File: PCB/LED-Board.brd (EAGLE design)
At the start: 71 x 34 mm, 33 parts, among them U1 ATSAMD11C14A-SSUT, U3 LDL1117S12R

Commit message: added button to pcbs and did some fixing
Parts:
- added R3: 2k, SparkFun-Resistors:1206
- added S1: MOMENTARY-SWITCH-SPST-SMD-6.0X3.5MM, SparkFun-Switches:TACTILE_SWITCH_SMD_6.0X3.5MM
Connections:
- removed net N$10: J3.4, U1.1
- new net N$13: J3.4, R3.2, S1.1, U1.1
- net 3.3V: now also S1.2
- net GND: now also R3.1
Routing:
- net N$13: track 0.00 -> 54.0 mm, vias 0 -> 3
- net 3.3V: track 55.3 -> 82.2 mm, vias 0 -> 4
- net N$10: track 20.9 -> 0.00 mm, vias 1 -> 0
- net VCC: track 58.8 -> 61.7 mm
- net N$2: track 24.5 -> 26.5 mm

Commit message: removed buttons.. not needed
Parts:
- removed R3: 2k, SparkFun-Resistors:1206
- removed S1: MOMENTARY-SWITCH-SPST-SMD-6.0X3.5MM, SparkFun-Switches:TACTILE_SWITCH_SMD_6.0X3.5MM
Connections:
- net 3.3V: no longer S1.2
- net GND: no longer R3.1
- net N$13: no longer R3.2, S1.1
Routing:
- net N$13: track 54.0 -> 20.9 mm, vias 3 -> 1
- net 3.3V: track 82.2 -> 62.5 mm, vias 4 -> 2

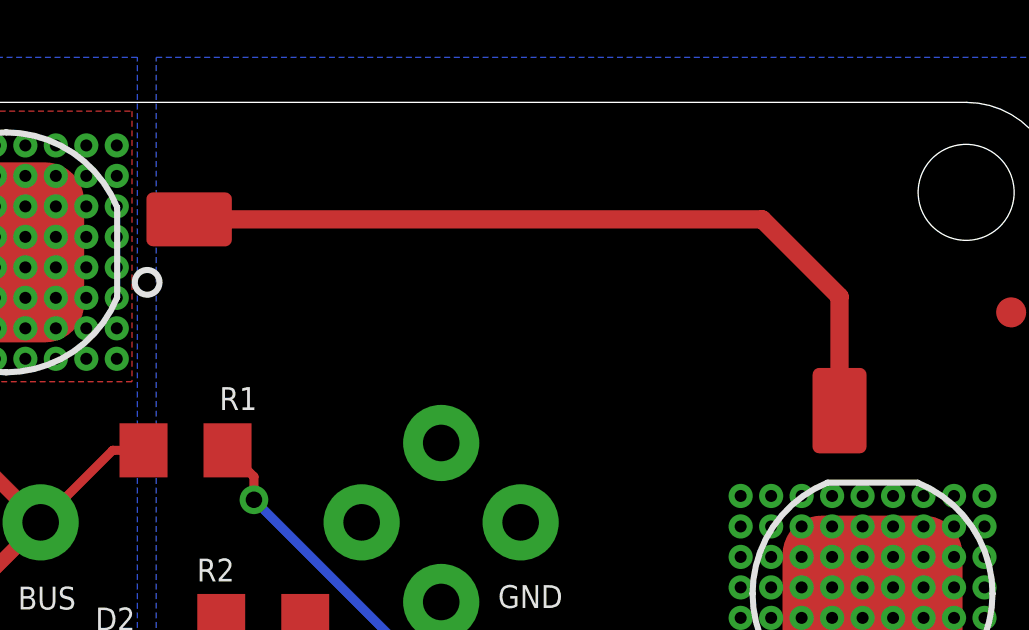
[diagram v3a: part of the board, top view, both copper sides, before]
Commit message: added b/tstop and b/restricted to write address on pcb
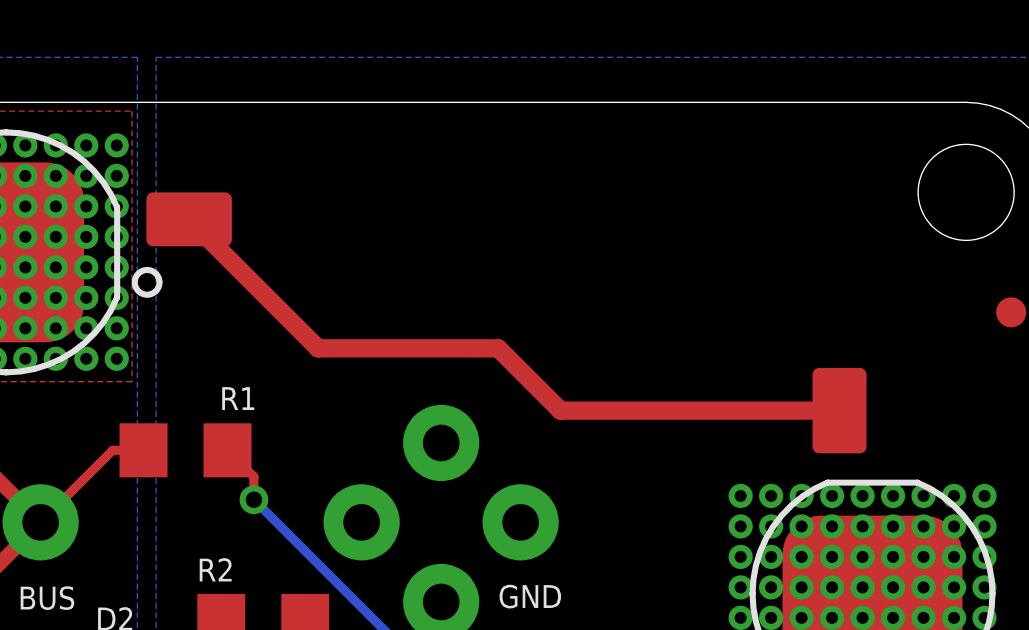
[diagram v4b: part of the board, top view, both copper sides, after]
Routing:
- net N$2: track 26.5 -> 24.3 mm
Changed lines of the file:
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@@
 <vertex x="9.31" y="15.241"/>
+</polygon>
+<polygon width="0.127" layer="30">
+<vertex x="47.141" y="33.207"/>
+<vertex x="64.496" y="33.207"/>
+<vertex x="64.496" y="26.99"/>
+<vertex x="47.141" y="26.99"/>
+</polygon>
+<polygon width="0.127" layer="41">
+<vertex x="64.459" y="33.207"/>
+<vertex x="47.104" y="33.207"/>
+<vertex x="47.104" y="26.99"/>
+<vertex x="64.459" y="26.99"/>
+</polygon>
+<polygon width="0.127" layer="29">
+<vertex x="64.459" y="33.207"/>
+<vertex x="47.104" y="33.207"/>
+<vertex x="47.104" y="26.99"/>
+<vertex x="64.459" y="26.99"/>
+</polygon>
+<polygon width="0.127" layer="42">
+<vertex x="64.459" y="26.993"/>
+<vertex x="47.104" y="26.993"/>
+<vertex x="47.104" y="33.21"/>
+<vertex x="64.459" y="33.21"/>
 </polygon>
 </plain>
@@
 <contactref element="LED-1" pad="C"/>
 <contactref element="LED-2" pad="A"/>
-<wire x1="42.1" y1="30.1" x2="61.203" y2="30.1" width="0.6096" layer="1"/>
-<wire x1="61.203" y1="30.1" x2="63.779" y2="27.524" width="0.6096" layer="1"/>
-<wire x1="63.779" y1="27.524" x2="63.779" y2="23.725" width="0.6096" layer="1"/>
-<wire x1="63.779" y1="23.725" x2="63.78" y2="23.724" width="0.6096" layer="1"/>
+<wire x1="52.404" y1="25.8" x2="46.4" y2="25.8" width="0.6096" layer="1"/>
+<wire x1="42.1" y1="30.1" x2="46.4" y2="25.8" width="0.6096" layer="1"/>
+<wire x1="54.48" y1="23.724" x2="63.78" y2="23.724" width="0.6096" layer="1"/>
+<wire x1="54.48" y1="23.724" x2="52.404" y2="25.8" width="0.6096" layer="1"/>
 </signal>
 <signal name="N$3">

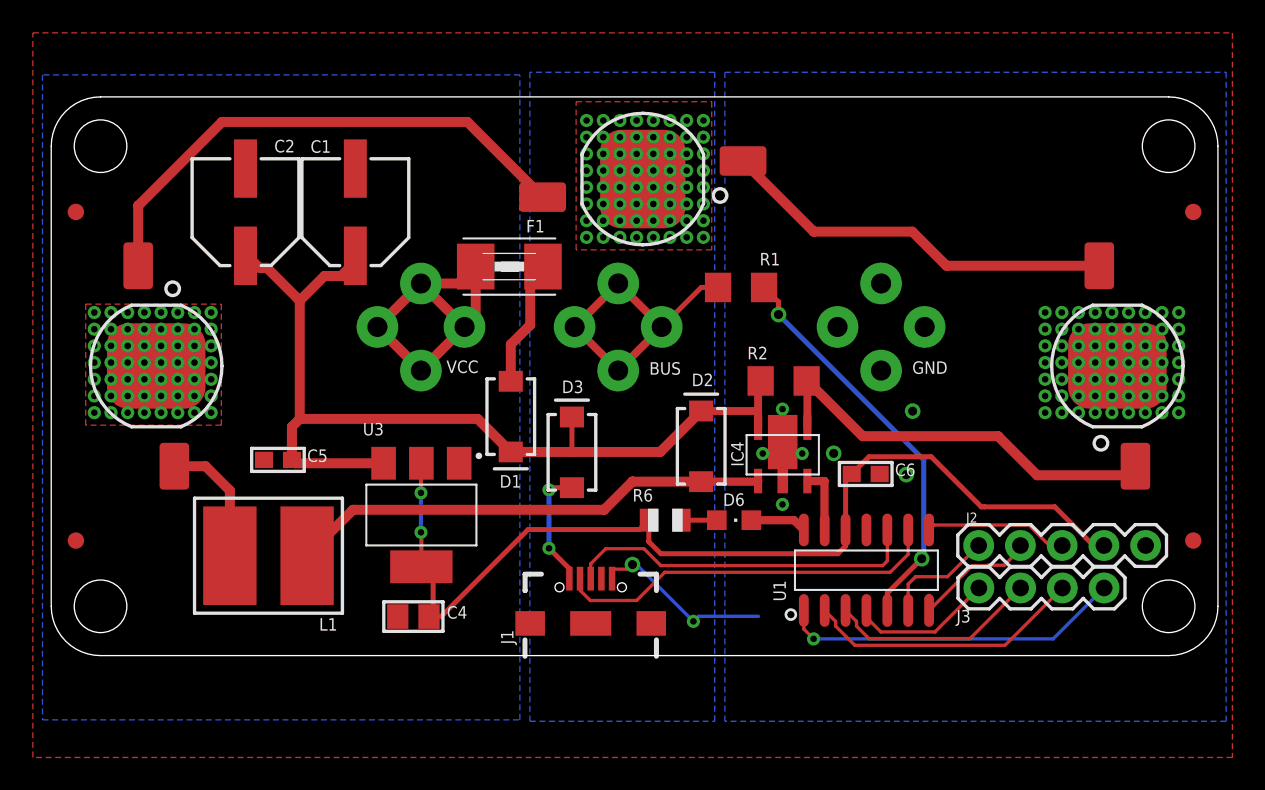
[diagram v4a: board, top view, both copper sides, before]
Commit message: increased led board bottom polygons for more equal heatsinks
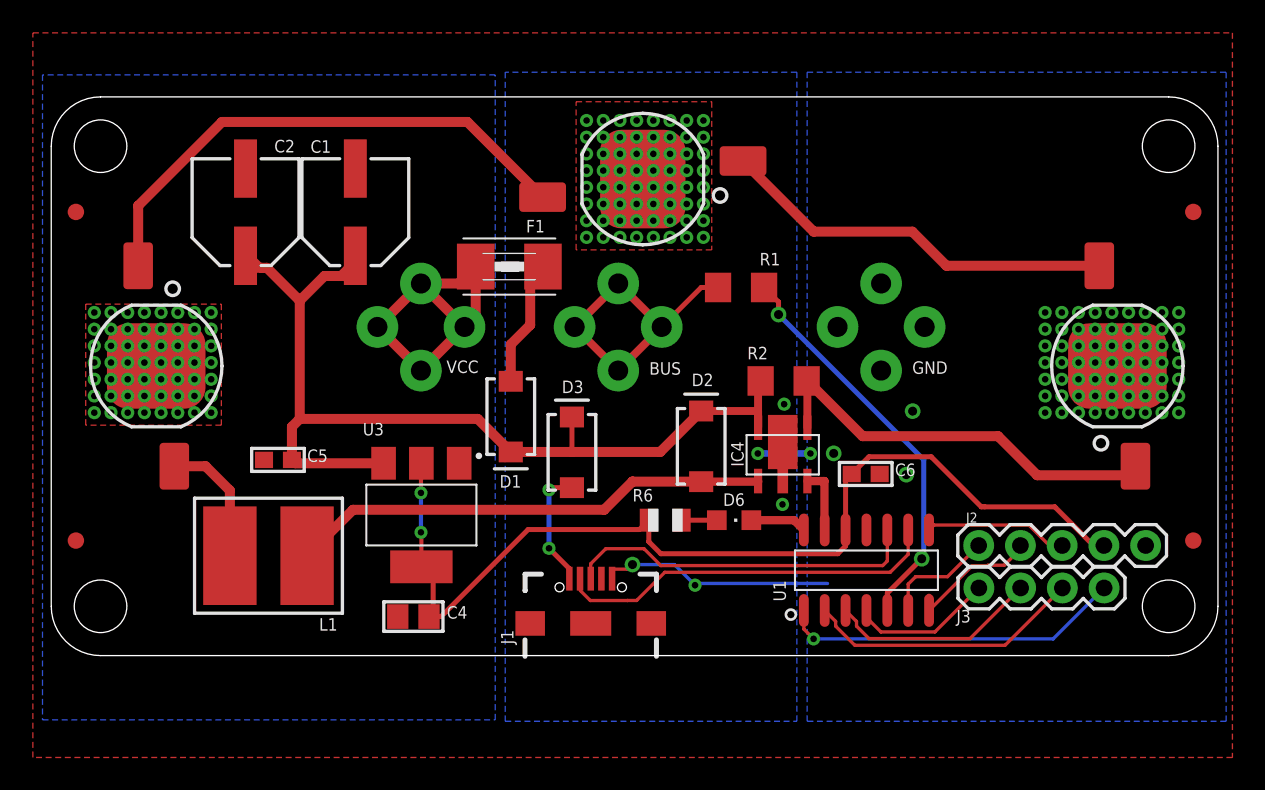
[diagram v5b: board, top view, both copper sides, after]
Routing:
- net GND: track 11.1 -> 17.5 mm
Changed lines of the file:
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@@
 <contactref element="GND-CLIP3" pad="CLIP-INPUT1"/>
 <polygon width="0.1524" layer="16" thermals="no" rank="2">
-<vertex x="41" y="-4"/>
-<vertex x="41" y="35.5"/>
+<vertex x="46" y="-4"/>
+<vertex x="46" y="35.5"/>
 <vertex x="71.5" y="35.5"/>
 <vertex x="71.5" y="-4"/>
@@
 <wire x1="34.227" y1="5.259" x2="35.0906" y2="5.259" width="0.2032" layer="1"/>
 <wire x1="35.0906" y1="5.259" x2="35.37" y2="5.5384" width="0.2032" layer="1"/>
-<wire x1="39.3832" y1="2.3888" x2="43.0408" y2="2.3888" width="0.2032" layer="16"/>
-<wire x1="39.3832" y1="2.3888" x2="39.0784" y2="2.084" width="0.2032" layer="16"/>
-<via x="39.0784" y="2.084" extent="1-16" drill="0.4"/>
+<wire x1="39.2832" y1="4.3888" x2="47.2408" y2="4.3888" width="0.2032" layer="16"/>
+<wire x1="39.2832" y1="4.3888" x2="39.1784" y2="4.284" width="0.2032" layer="16"/>
+<via x="39.1784" y="4.284" extent="1-16" drill="0.4"/>
 <contactref element="C2" pad="-"/>
-<wire x1="35.37" y1="5.5384" x2="35.624" y2="5.5384" width="0.2032" layer="16"/>
-<wire x1="35.624" y1="5.5384" x2="39.0784" y2="2.084" width="0.2032" layer="16"/>
-<via x="45.7" y="12.3" extent="1-16" drill="0.4"/>
-<via x="43.3" y="12.3" extent="1-16" drill="0.4"/>
-<via x="44.5" y="15" extent="1-16" drill="0.4"/>
+<wire x1="35.37" y1="5.5384" x2="37.924" y2="5.5384" width="0.2032" layer="16"/>
+<wire x1="37.924" y1="5.5384" x2="39.1784" y2="4.284" width="0.2032" layer="16"/>
+<via x="46.2" y="12.3" extent="1-16" drill="0.4"/>
+<via x="43" y="12.3" extent="1-16" drill="0.4"/>
+<via x="44.6" y="15.3" extent="1-16" drill="0.4"/>
 <via x="44.5" y="9.2" extent="1-16" drill="0.4"/>
 <contactref element="J2" pad="1"/>
+<wire x1="46.2" y1="12.3" x2="43" y2="12.3" width="0.4064" layer="16"/>
 </signal>
 <signal name="LED-">
@@
 <vertex x="-0.532" y="35.34"/>
 <vertex x="-0.532" y="-3.91"/>
-<vertex x="28.518" y="-3.91"/>
-<vertex x="28.518" y="35.34"/>
+<vertex x="27.018" y="-3.91"/>
+<vertex x="27.018" y="35.34"/>
 </polygon>
 <contactref element="LED-3" pad="S"/>
@@
 <via x="32.576" y="32.564" extent="1-16" drill="0.4"/>
 <polygon width="0.1524" layer="16" thermals="no" rank="3">
-<vertex x="29.127" y="35.5"/>
-<vertex x="29.127" y="-4"/>
-<vertex x="40.373" y="-4"/>
-<vertex x="40.373" y="35.5"/>
+<vertex x="27.627" y="35.5"/>
+<vertex x="27.627" y="-4"/>
+<vertex x="45.373" y="-4"/>
+<vertex x="45.373" y="35.5"/>
 </polygon>
 <polygon width="0.127" layer="1" thermals="no">
